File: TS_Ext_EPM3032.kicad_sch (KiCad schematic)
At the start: 56 parts, among them J1 JTAG, J2 CD_IN, J3 System Ext, J4 AUDIO OUT, J5 AudioJack3_SwitchTR, Q1 BC547, Q2 BC547, Q3 BC547, U1 EPM3064ALC44, U2 AMS1117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

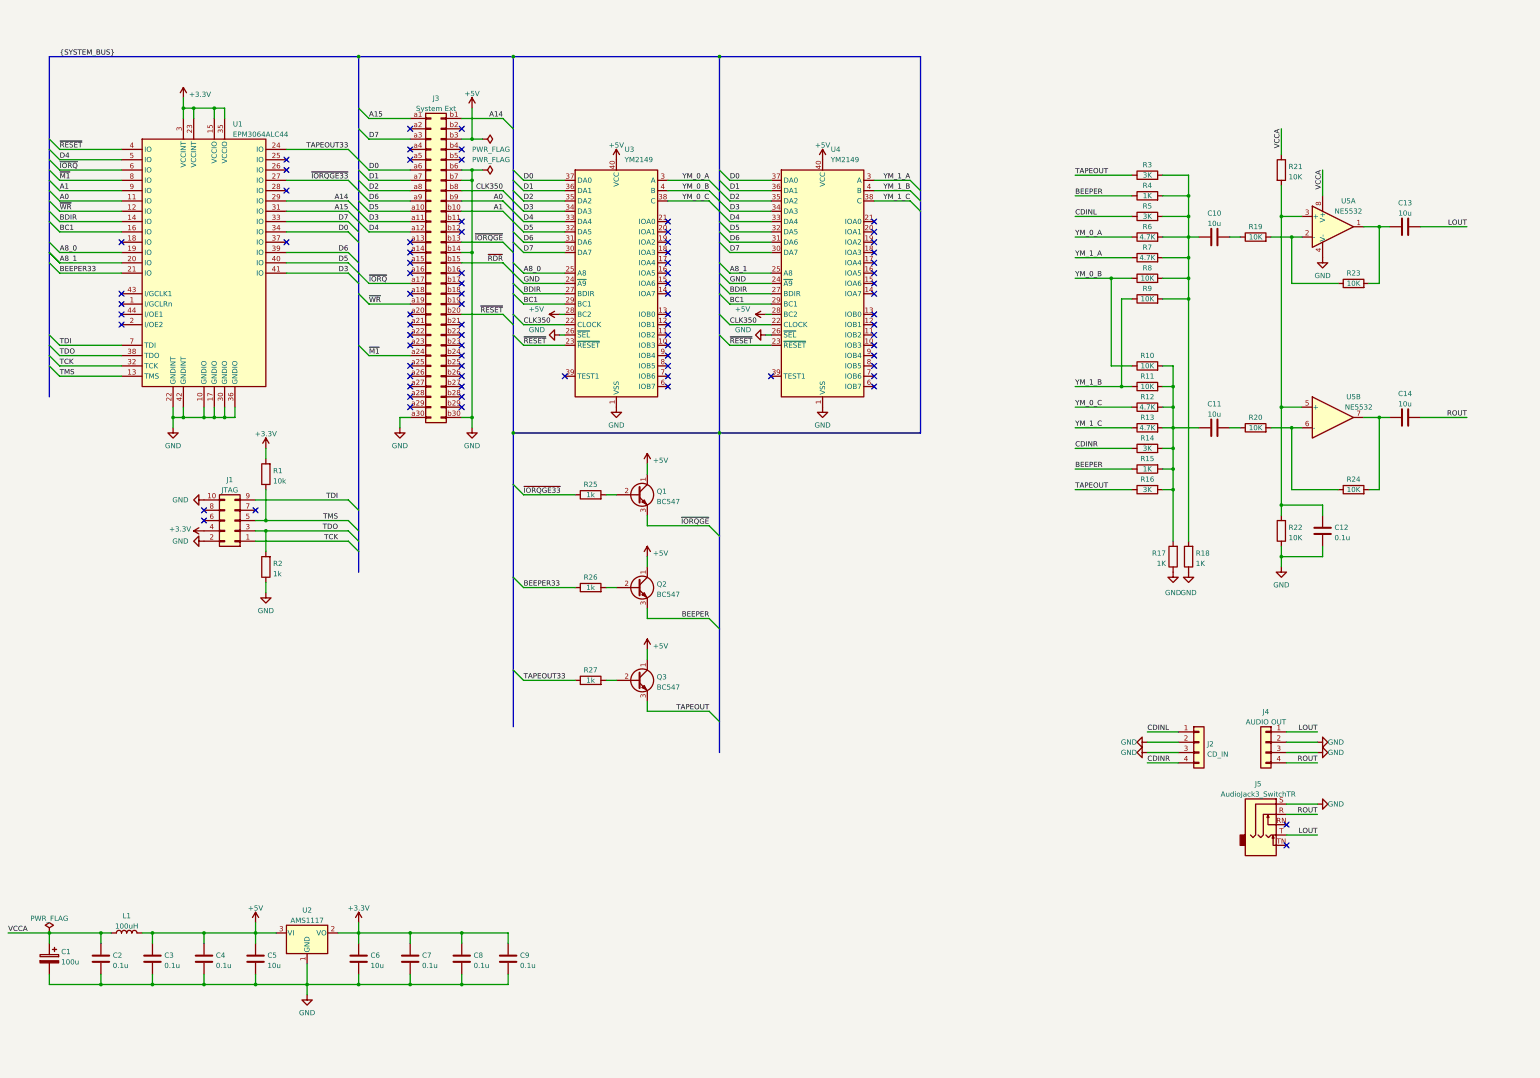
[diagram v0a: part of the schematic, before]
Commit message: * Bump to version 1.0 * BOM, schematics and gerbers added
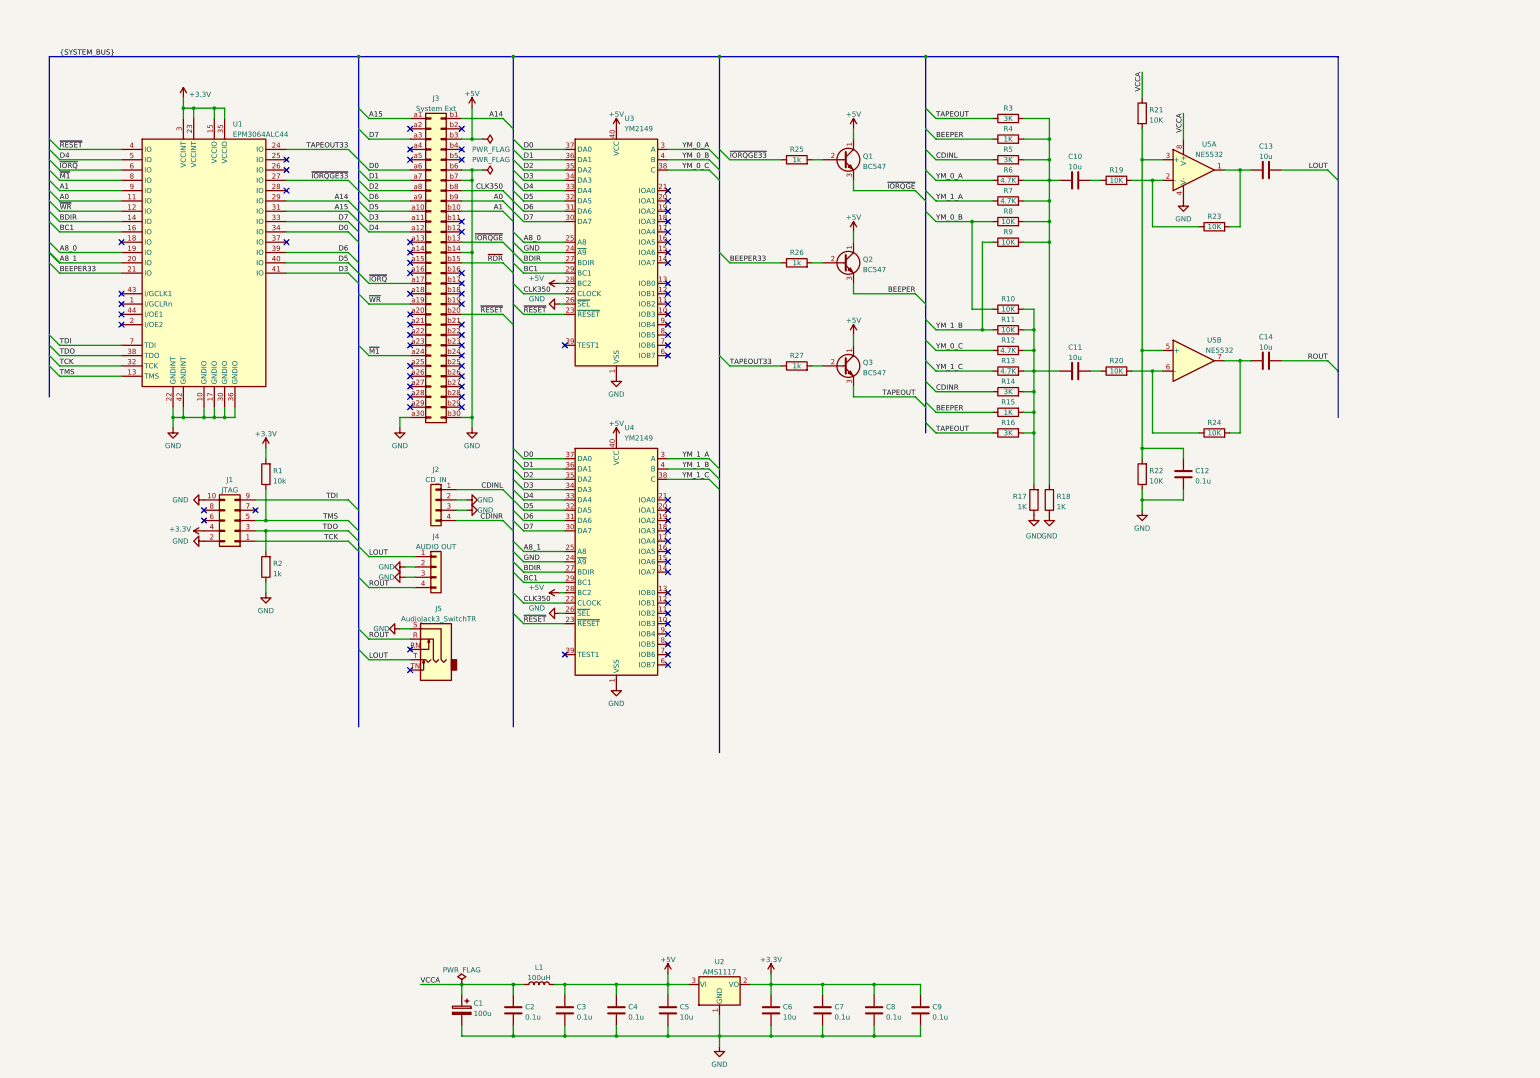
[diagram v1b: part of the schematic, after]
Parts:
- LOGO1: now left out of the parts list
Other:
- moved on the sheet: C1, C10, C11, C12, C13, C14, C2, C3, C4, C5, C6, C7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

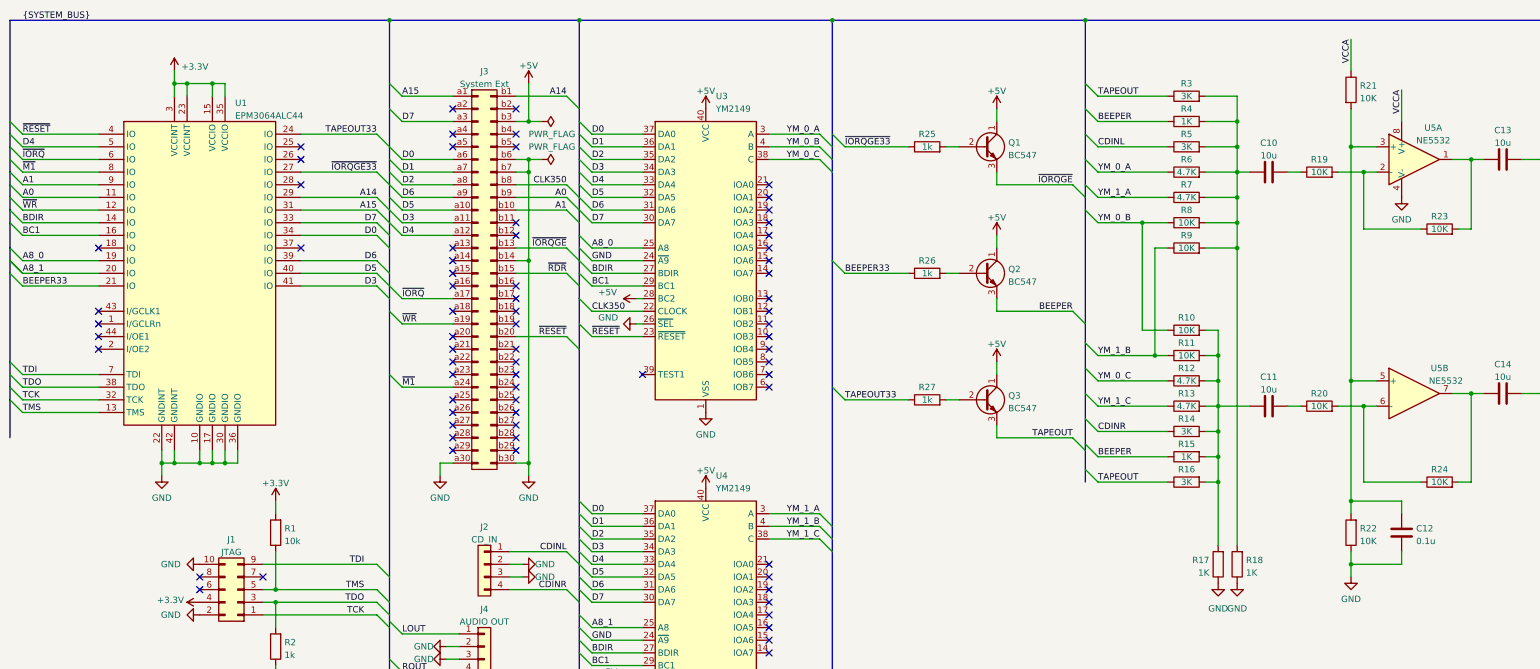
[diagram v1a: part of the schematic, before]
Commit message: Remove transistors, reorganize folders
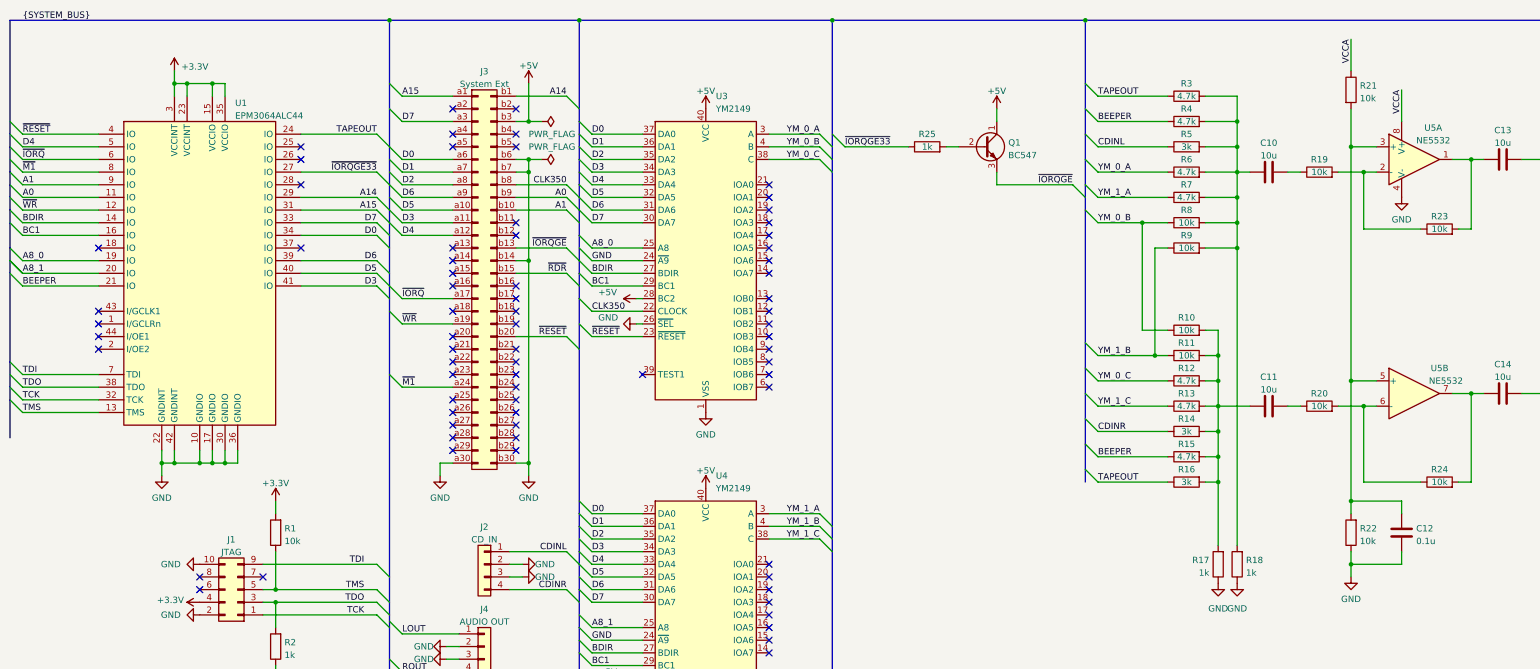
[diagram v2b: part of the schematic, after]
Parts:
- removed Q2, Q3: BC547, Package_TO_SOT_THT:TO-92_Inline, symbol Transistor_BJT:BC547
- removed R26, R27: 1k, Resistor_THT:R_Axial_DIN0204_L3.6mm_D1.6mm_P7.62mm_Horizontal, symbol Device:R
- R10, R11, R19, R20, R21, R22, R23, R24, R8, R9: value 10K -> 10k
- R12, R13, R6, R7: value 4.7K -> 4.7k
- R14, R16, R5: value 3K -> 3k
- R15, R4: value 1K -> 4.7k
- R17, R18: value 1K -> 1k
- R3: value 3K -> 4.7k
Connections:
- net BEEPER33 is gone; now on net BEEPER: U1.21 (IO)
- net TAPEOUT33 is gone; now on net TAPEOUT: U1.24 (IO)

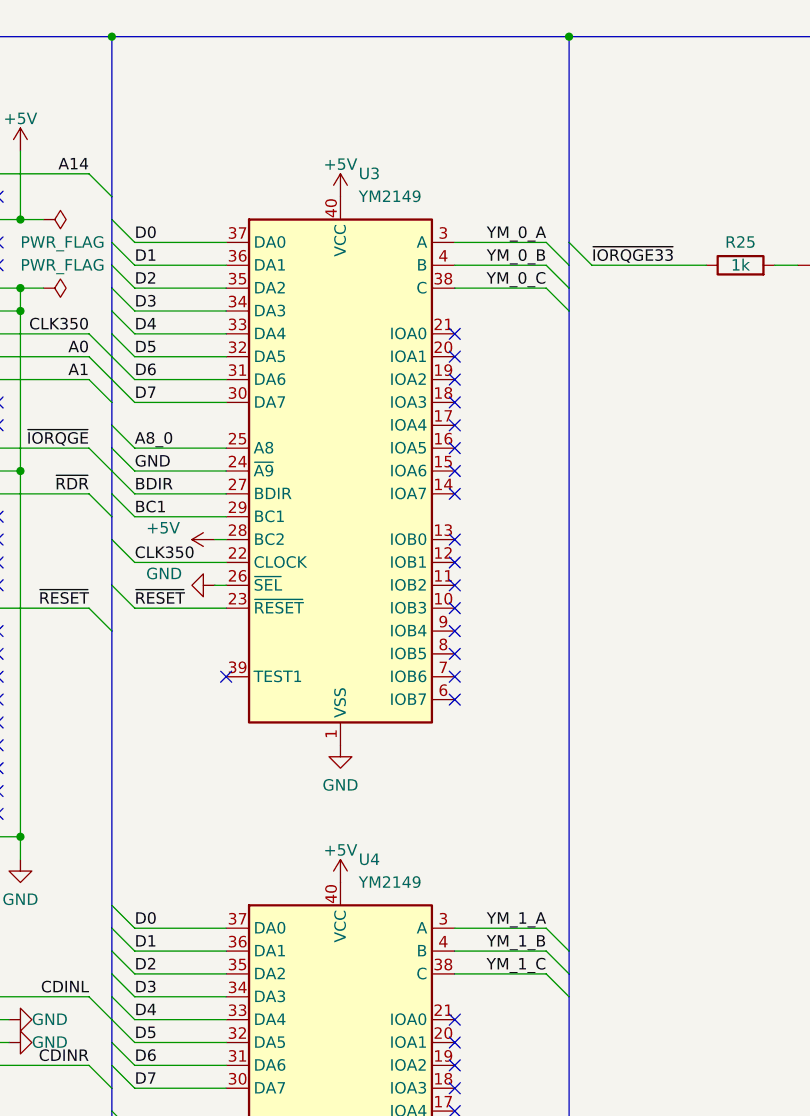
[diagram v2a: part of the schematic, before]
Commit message: Fix YM2149F symbol
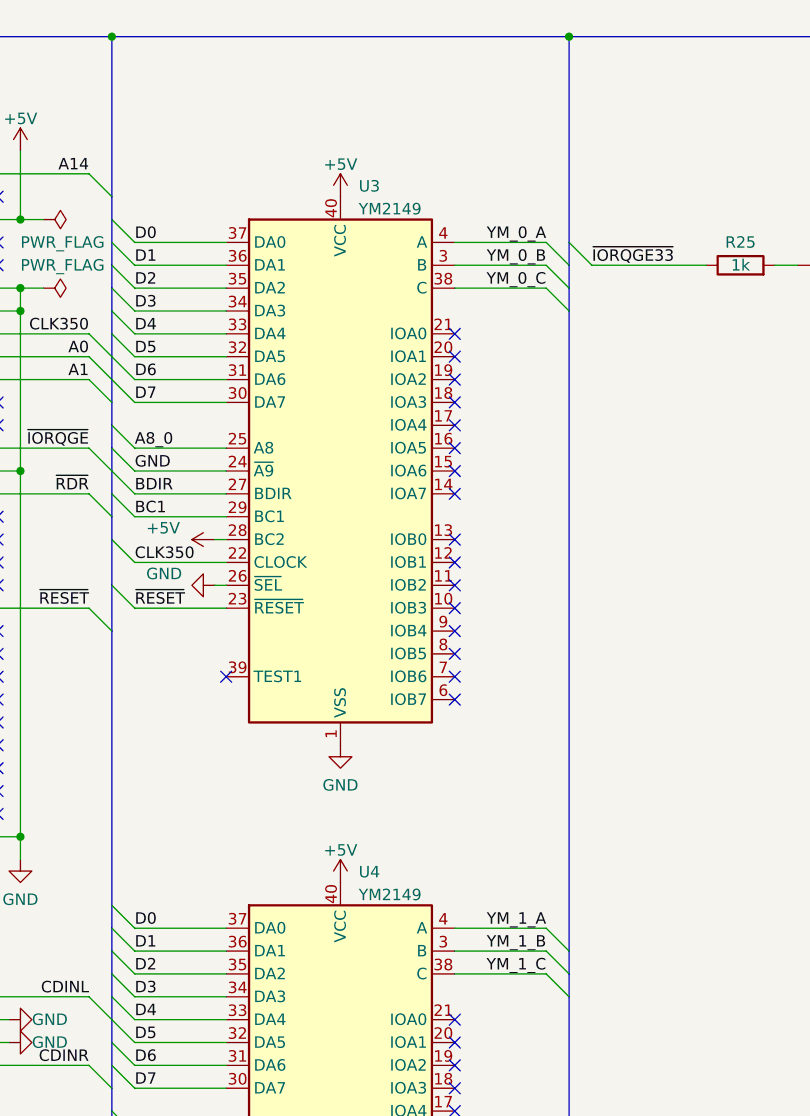
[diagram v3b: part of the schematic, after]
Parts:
- U3, U4: symbol Audio:YM2149 -> TS:YM2149
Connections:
- net YM_0_A: now also U3.4 (A); no longer U3.3 (A)
- net YM_0_B: now also U3.3 (B); no longer U3.4 (B)
- net YM_1_A: now also U4.4 (A); no longer U4.3 (A)
- net YM_1_B: now also U4.3 (B); no longer U4.4 (B)
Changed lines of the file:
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@@
   (title_block
     (title "TurboSound Extension Card EPM3032")
-    (date "2022-10-26")
-    (rev "1.1")
+    (date "2022-11-06")
+    (rev "1.2")
     (company "ponchick")
     (comment 1 "Original schematic and firmware by MikhaelK")
@@
     (pin "1")
   )
-  (symbol (lib_id "Audio:YM2149") (at 165.1 73.66 0) (unit 1)
+  (symbol (lib_id "TS:YM2149") (at 165.1 73.66 0) (unit 1)
     (in_bom yes) (on_board yes) (fields_autoplaced)
-    (property "Reference" "U3" (id 0) (at 167.1194 40.64 0)
+    (property "Reference" "U3" (id 0) (at 167.1194 42.0202 0)
       (effects (font (size 1.27 1.27)) (justify left))
     )
-    (property "Value" "YM2149" (id 1) (at 167.1194 43.18 0)
+    (property "Value" "YM2149" (id 1) (at 167.1194 44.5571 0)
       (effects (font (size 1.27 1.27)) (justify left))
     )
@@
     (pin "2")
   )
-  (symbol (lib_id "Audio:YM2149") (at 165.1 149.86 0) (unit 1)
+  (symbol (lib_id "TS:YM2149") (at 165.1 149.86 0) (unit 1)
     (in_bom yes) (on_board yes) (fields_autoplaced)
-    (property "Reference" "U4" (id 0) (at 167.1194 116.84 0)
+    (property "Reference" "U4" (id 0) (at 167.1194 118.2202 0)
       (effects (font (size 1.27 1.27)) (justify left))
     )
-    (property "Value" "YM2149" (id 1) (at 167.1194 119.38 0)
+    (property "Value" "YM2149" (id 1) (at 167.1194 120.7571 0)
       (effects (font (size 1.27 1.27)) (justify left))
     )
